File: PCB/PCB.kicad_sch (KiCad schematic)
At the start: 17 parts, among them SW1 SW_Push, SW2 SW_Push, SW3 SW_Push, SW4 SW_Push, SW5 SW_Push, SW6 SW_Push, U1 NodeMCU_1.0_(ESP-12E)

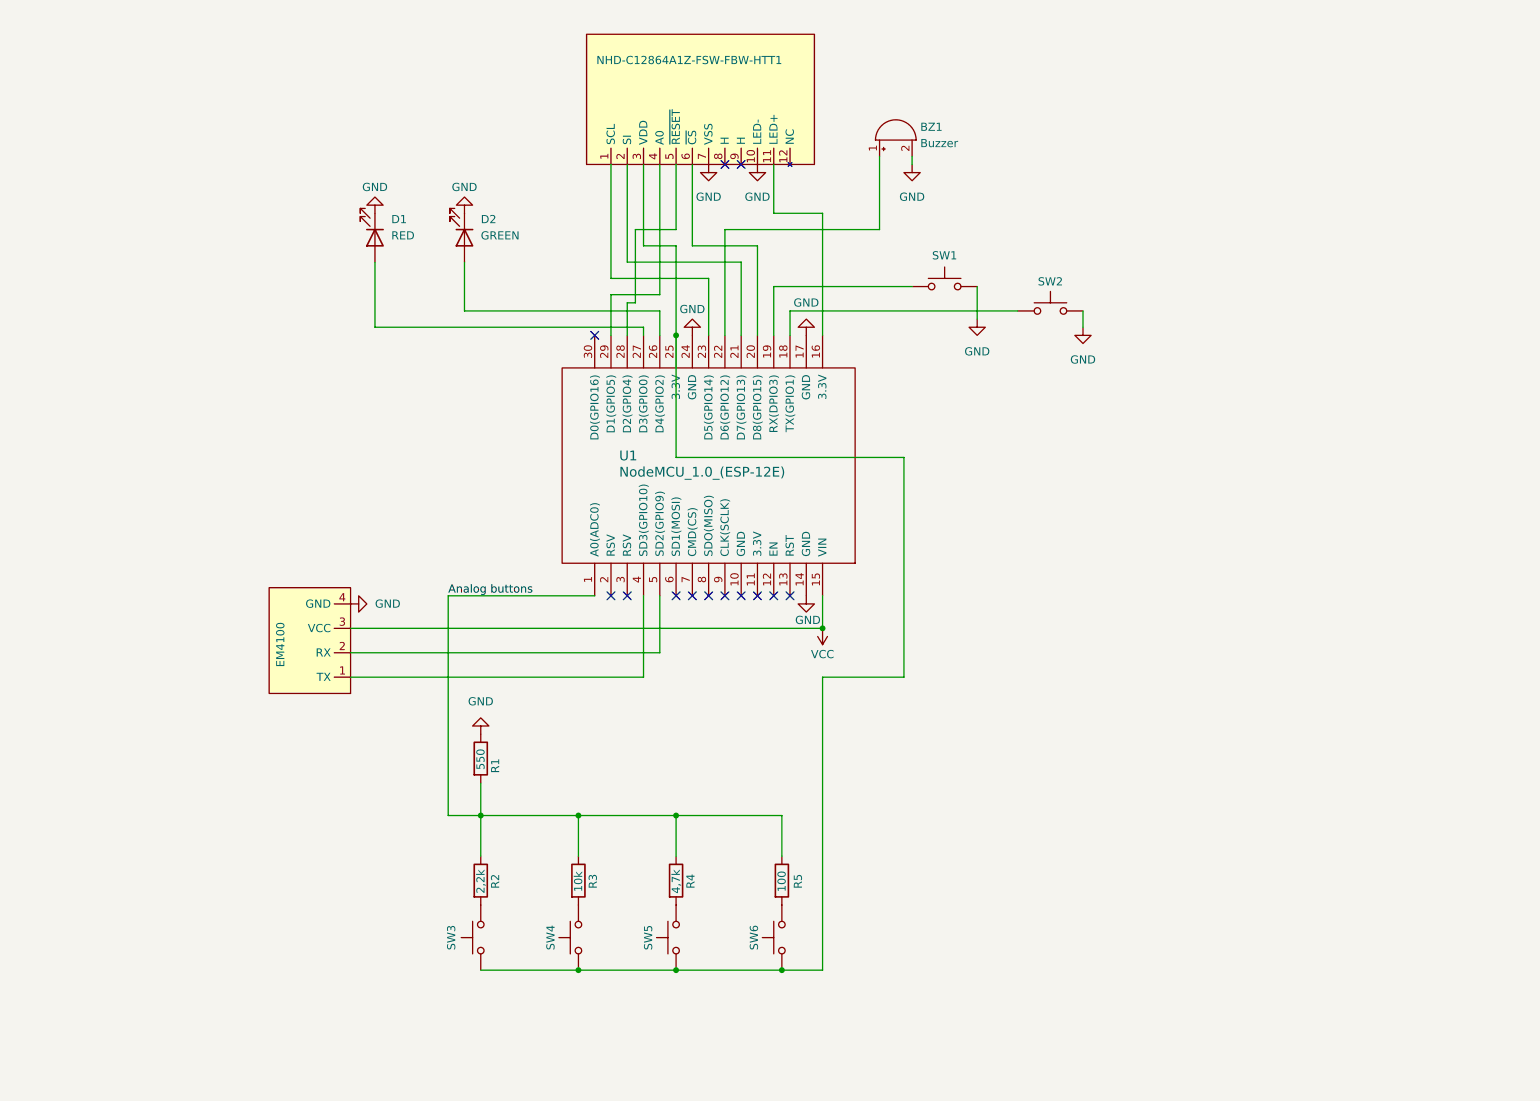
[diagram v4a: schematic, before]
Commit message: Updated schematic after CMZ feedback
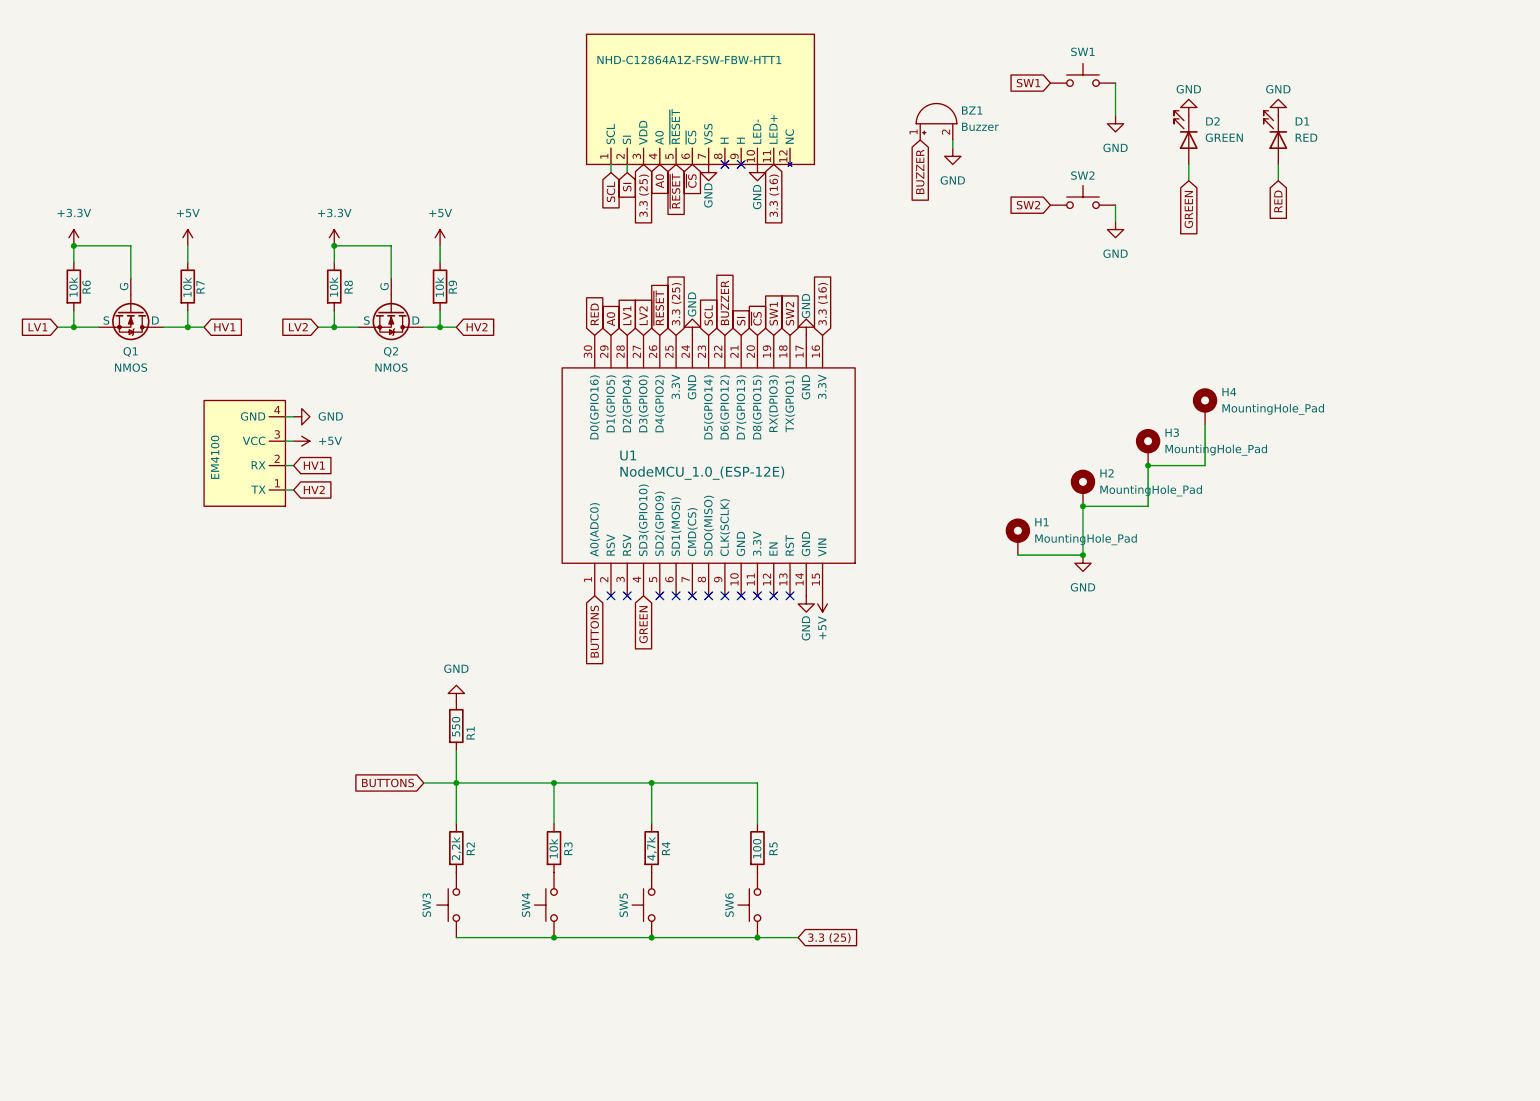
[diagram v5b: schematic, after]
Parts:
- added H1, H2, H3, H4: MountingHole_Pad, MountingHole:MountingHole_3.2mm_M3, symbol Mechanical:MountingHole_Pad
- added Q1, Q2: NMOS, symbol Simulation_SPICE:NMOS
- added R6, R7, R8, R9: 10k, symbol Device:R
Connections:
- net GND: now also H1.1, H2.1, H3.1, H4.1
- net LV2: now reaches U1.27 (D3(GPIO0))
- net LV2: now also Q2.3 (S), R8.2; no longer D1.2 (A)
- net SW1: now reaches SW1.1, U1.19 (RX(DPIO3))
- net SCL: now reaches NHD-C12864A1Z-FSW-FBW-HTT1.1 (SCL), U1.23 (D5(GPIO14))
- net 3.3 (16): now reaches NHD-C12864A1Z-FSW-FBW-HTT1.11 (LED+), U1.16 (3.3V)
- net SI: now reaches NHD-C12864A1Z-FSW-FBW-HTT1.2 (SI), U1.21 (D7(GPIO13))
- net 3.3 (25): now reaches NHD-C12864A1Z-FSW-FBW-HTT1.3 (VDD), SW3.1, SW4.1, SW5.1, SW6.1, U1.25 (3.3V)
- net A0: now reaches NHD-C12864A1Z-FSW-FBW-HTT1.4 (A0), U1.29 (D1(GPIO5))
- net LV1: now reaches U1.28 (D2(GPIO4))
- net LV1: now also Q1.3 (S), R6.2; no longer NHD-C12864A1Z-FSW-FBW-HTT1.5 (~{RESET})
- net ~{CS}: now reaches NHD-C12864A1Z-FSW-FBW-HTT1.6 (~{CS}), U1.20 (D8(GPIO15))
- net SW2: now reaches SW2.1, U1.18 (TX(GPIO1))
- net BUZZER: now reaches BZ1.1 (+), U1.22 (D6(GPIO12))
- net GREEN: now reaches U1.4 (SD3(GPIO10))
- net GREEN: now also D2.2 (A); no longer EM4100.1 (TX)
- net at U1.5 (SD2(GPIO9)): no longer EM4100.2 (RX)
- net ~{RESET}: now reaches U1.26 (D4(GPIO2))
- net ~{RESET}: now also NHD-C12864A1Z-FSW-FBW-HTT1.5 (~{RESET}); no longer D2.2 (A)
- net RED: now reaches U1.30 (D0(GPIO16))
- net RED: now also D1.2 (A)
- net Analog buttons renamed BUTTONS
- net VCC renamed +5V
- net +5V: now also R7.1, R9.1
- new net +3.3V: Q1.2 (G), Q2.2 (G), R6.1, R8.1
- new net HV1: EM4100.2 (RX), Q1.1 (D), R7.2
- new net HV2: EM4100.1 (TX), Q2.1 (D), R9.2
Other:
- moved on the sheet: BZ1, D1, D2, EM4100, R1, R2, R3, R4, R5, SW1, SW2, SW3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

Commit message: drawn new PCB based on feedback
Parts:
- Q1, Q2: footprint (none) -> Package_TO_SOT_THT:TO-92
- R1, R2, R3, R4, R5: footprint Resistor_SMD:R_1206_3216Metric_Pad1.30x1.75mm_HandSolder -> Resistor_THT:R_Axial_DIN0207_L6.3mm_D2.5mm_P7.62mm_Horizontal
- R6, R7, R8, R9: footprint (none) -> Resistor_THT:R_Axial_DIN0207_L6.3mm_D2.5mm_P7.62mm_Horizontal
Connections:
- net 3.3 (16) is gone; now on net +3.3V: NHD-C12864A1Z-FSW-FBW-HTT1.11 (LED+), U1.16 (3.3V)
- net 3.3 (25) is gone; now on net +3.3V: NHD-C12864A1Z-FSW-FBW-HTT1.3 (VDD), SW3.1, SW4.1, SW5.1, SW6.1, U1.25 (3.3V)
- net +3.3V: now also U1.11 (3.3V)
- net GND: now also U1.10 (GND)
- no-connect marks 13 -> 12
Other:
- moved on the sheet: H1, H2, H3, H4

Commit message: Fixed all errors and drawn tracks on 2nd layer
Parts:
- H1: footprint MountingHole:MountingHole_3.2mm_M3 -> MountingHole:MountingHole_3.2mm_M3_Pad
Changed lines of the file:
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@@
+	(wire
+		(pts
+			(xy 102.87 76.2) (xy 102.87 73.66)
+		)
+		(stroke
+			(width 0)
+			(type default)
+		)
+	)
+	(wire
+		(pts
+			(xy 95.25 63.5) (xy 86.36 63.5)
+		)
+		(stroke
+			(width 0)
+			(type default)
+		)
+	)
+	(wire
+		(pts
+			(xy 80.01 90.17) (xy 78.74 90.17)
+		)
+		(stroke
+			(width 0)
+			(type default)
+		)
+	)
+	(wire
+		(pts
+			(xy 246.38 100.33) (xy 224.79 100.33)
+		)
+		(stroke
+			(width 0)
+			(type default)
+		)
+	)
+	(wire
+		(pts
+			(xy 80.01 93.98) (xy 78.74 93.98)
+		)
+		(stroke
+			(width 0)
+			(type default)
+		)
+	)
 	(wire
 		(pts
 			(xy 78.74 97.79) (xy 80.01 97.79)
-		)
-		(stroke
-			(width 0)
-			(type default)
-		)
-	)
-	(wire
-		(pts
-			(xy 102.87 76.2) (xy 102.87 73.66)
-		)
-		(stroke
-			(width 0)
-			(type default)
-		)
-	)
-	(wire
-		(pts
-			(xy 95.25 63.5) (xy 86.36 63.5)
-		)
-		(stroke
-			(width 0)
-			(type default)
-		)
-	)
-	(wire
-		(pts
-			(xy 80.01 90.17) (xy 78.74 90.17)
-		)
-		(stroke
-			(width 0)
-			(type default)
-		)
-	)
-	(wire
-		(pts
-			(xy 246.38 100.33) (xy 224.79 100.33)
-		)
-		(stroke
-			(width 0)
-			(type default)
-		)
-	)
-	(wire
-		(pts
-			(xy 80.01 93.98) (xy 78.74 93.98)
 		)
 		(stroke
@@
 			)
 		)
-		(property "Footprint" "MountingHole:MountingHole_3.2mm_M3"
+		(property "Footprint" "MountingHole:MountingHole_3.2mm_M3_Pad"
 			(at 184.15 96.52 0)
 			(effects

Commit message: inital final
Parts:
- H2, H3, H4: footprint MountingHole:MountingHole_3.2mm_M3 -> MountingHole:MountingHole_3.2mm_M3_Pad
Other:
- moved on the sheet: H1
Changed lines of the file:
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@@
 	(title_block
 		(title "Meeting display")
-		(date "2024-04-24")
+		(date "2024-04-25")
 		(rev "0.3")
 		(company "KTH")
@@
 	)
 	(junction
-		(at 86.36 63.5)
+		(at 160.02 63.5)
 		(diameter 0)
 		(color 0 0 0 0)
 	)
 	(junction
-		(at 152.4 171.45)
+		(at 86.36 63.5)
 		(diameter 0)
 		(color 0 0 0 0)
 	)
 	(junction
-		(at 45.72 76.2)
+		(at 152.4 171.45)
 		(diameter 0)
 		(color 0 0 0 0)
 	)
 	(junction
-		(at 165.1 66.04)
+		(at 45.72 76.2)
 		(diameter 0)
 		(color 0 0 0 0)
@@
 	(wire
 		(pts
-			(xy 184.15 100.33) (xy 204.47 100.33)
-		)
-		(stroke
-			(width 0)
-			(type default)
-		)
-	)
-	(wire
-		(pts
-			(xy 165.1 67.31) (xy 165.1 66.04)
+			(xy 182.88 100.33) (xy 204.47 100.33)
 		)
 		(stroke
@@
 	(wire
 		(pts
-			(xy 165.1 66.04) (xy 160.02 66.04)
-		)
-		(stroke
-			(width 0)
-			(type default)
-		)
-	)
-	(wire
-		(pts
 			(xy 83.82 76.2) (xy 86.36 76.2)
 		)
@@
 	(wire
 		(pts
-			(xy 184.15 99.06) (xy 184.15 100.33)
+			(xy 182.88 99.06) (xy 182.88 100.33)
 		)
 		(stroke
@@
 	(wire
 		(pts
-			(xy 160.02 66.04) (xy 160.02 77.47)
+			(xy 160.02 63.5) (xy 160.02 77.47)
 		)
 		(stroke
@@
 	(wire
 		(pts
+			(xy 162.56 73.66) (xy 162.56 77.47)
+		)
+		(stroke
+			(width 0)
+			(type default)
+		)
+	)
+	(wire
+		(pts
 			(xy 120.65 147.32) (xy 120.65 153.67)
 		)
@@
 	)
 	(symbol
-		(lib_id "power:PWR_FLAG")
-		(at 165.1 67.31 180)
-		(unit 1)
-		(exclude_from_sim no)
-		(in_bom yes)
-		(on_board yes)
-		(dnp no)
-		(property "Reference" "#FLG02"
-			(at 165.1 69.215 0)
-			(effects
-				(font
-					(size 1.27 1.27)
-				)
-				(hide yes)
-			)
-		)
-		(property "Value" "PWR_FLAG"
-			(at 168.656 71.628 0)
-			(effects
-				(font
-					(size 1.27 1.27)
-				)
-			)
-		)
-		(property "Footprint" ""
-			(at 165.1 67.31 0)
-			(effects
-				(font
-					(size 1.27 1.27)
-				)
-				(hide yes)
-			)
-		)
-		(property "Datasheet" "~"
-			(at 165.1 67.31 0)
-			(effects
-				(font
-					(size 1.27 1.27)
-				)
-				(hide yes)
-			)
-		)
-		(property "Description" "Special symbol for telling ERC where power comes from"
-			(at 165.1 67.31 0)
-			(effects
-				(font
-					(size 1.27 1.27)
-				)
-				(hide yes)
-			)
-		)
-		(pin "1"
-		)
-		(instances
-			(project "PCB"
-				(path "/95b5e99e-302e-4222-afa1-0faa09b15eb9"
-					(reference "#FLG02")
-					(unit 1)
-				)
-			)
-		)
-	)
-	(symbol
 		(lib_id "power:+5V")
 		(at 63.5 63.5 0)
@@
 	(symbol
 		(lib_id "power:+3.3V")
-		(at 162.56 77.47 0)
+		(at 162.56 73.66 0)
 		(unit 1)
 		(exclude_from_sim no)
@@
 		(dnp no)
 		(property "Reference" "#PWR018"
-			(at 162.56 81.28 0)
+			(at 162.56 77.47 0)
 			(effects
 				(font
@@
 		)
 		(property "Value" "+3.3V"
-			(at 162.56 71.882 90)
+			(at 162.56 68.072 90)
 			(effects
 				(font
@@
 		)
 		(property "Footprint" ""
-			(at 162.56 77.47 0)
+			(at 162.56 73.66 0)
 			(effects
 				(font
@@
 		)
 		(property "Datasheet" ""
-			(at 162.56 77.47 0)
+			(at 162.56 73.66 0)
 			(effects
 				(font
@@
 		)
 		(property "Description" "Power symbol creates a global label with name \"+3.3V\""
-			(at 162.56 77.47 0)
+			(at 162.56 73.66 0)
 			(effects
 				(font
@@
 	(symbol
 		(lib_id "Mechanical:MountingHole_Pad")
-		(at 184.15 96.52 0)
+		(at 182.88 96.52 0)
 		(unit 1)
 		(exclude_from_sim yes)
@@
 		(dnp no)
 		(property "Reference" "H1"
-			(at 186.69 93.9799 0)
+			(at 185.42 93.9799 0)
 			(effects
 				(font
@@
 		)
 		(property "Value" "MountingHole_Pad"
-			(at 186.69 96.5199 0)
+			(at 185.42 96.5199 0)
 			(effects
 				(font
@@
 		)
 		(property "Footprint" "MountingHole:MountingHole_3.2mm_M3_Pad"
-			(at 184.15 96.52 0)
+			(at 182.88 96.52 0)
 			(effects
 				(font
@@
 		)
 		(property "Datasheet" "~"
-			(at 184.15 96.52 0)
+			(at 182.88 96.52 0)
 			(effects
 				(font
@@
 		)
 		(property "Description" "Mounting Hole with connection"
-			(at 184.15 96.52 0)
+			(at 182.88 96.52 0)
 			(effects
 				(font
@@
 			)
 		)
-		(property "Footprint" "MountingHole:MountingHole_3.2mm_M3"
+		(property "Footprint" "MountingHole:MountingHole_3.2mm_M3_Pad"
 			(at 246.38 82.55 0)
 			(effects
@@
 			)
 		)
-		(property "Footprint" "MountingHole:MountingHole_3.2mm_M3"
+		(property "Footprint" "MountingHole:MountingHole_3.2mm_M3_Pad"
 			(at 224.79 85.09 0)
 			(effects
@@
 	)
 	(symbol
+		(lib_id "power:PWR_FLAG")
+		(at 160.02 63.5 0)
+		(unit 1)
+		(exclude_from_sim no)
+		(in_bom yes)
+		(on_board yes)
+		(dnp no)
+		(property "Reference" "#FLG02"
+			(at 160.02 61.595 0)
+			(effects
+				(font
+					(size 1.27 1.27)
+				)
+				(hide yes)
+			)
+		)
+		(property "Value" "PWR_FLAG"
+			(at 163.83 59.182 0)
+			(effects
+				(font
+					(size 1.27 1.27)
+				)
+			)
+		)
+		(property "Footprint" ""
+			(at 160.02 63.5 0)
+			(effects
+				(font
+					(size 1.27 1.27)
+				)
+				(hide yes)
+			)
+		)
+		(property "Datasheet" "~"
+			(at 160.02 63.5 0)
+			(effects
+				(font
+					(size 1.27 1.27)
+				)
+				(hide yes)
+			)
+		)
+		(property "Description" "Special symbol for telling ERC where power comes from"
+			(at 160.02 63.5 0)
+			(effects
+				(font
+					(size 1.27 1.27)
+				)
+				(hide yes)
+			)
+		)
+		(pin "1"
+		)
+		(instances
+			(project "PCB"
+				(path "/95b5e99e-302e-4222-afa1-0faa09b15eb9"
+					(reference "#FLG02")
+					(unit 1)
+				)
+			)
+		)
+	)
+	(symbol
 		(lib_id "power:GND")
-		(at 165.1 66.04 90)
+		(at 160.02 63.5 90)
 		(unit 1)
 		(exclude_from_sim no)
@@
 		(dnp no)
 		(property "Reference" "#PWR02"
-			(at 171.45 66.04 0)
+			(at 166.37 63.5 0)
 			(effects
 				(font
@@
 		)
 		(property "Value" "GND"
-			(at 170.18 66.04 90)
+			(at 165.1 63.5 90)
 			(effects
 				(font
@@
 		)
 		(property "Footprint" ""
-			(at 165.1 66.04 0)
+			(at 160.02 63.5 0)
 			(effects
 				(font
@@
 		)
 		(property "Datasheet" ""
-			(at 165.1 66.04 0)
+			(at 160.02 63.5 0)
 			(effects
 				(font
@@
 		)
 		(property "Description" "Power symbol creates a global label with name \"GND\" , ground"
-			(at 165.1 66.04 0)
+			(at 160.02 63.5 0)
 			(effects
 				(font
@@
 			)
 		)
-		(property "Footprint" "MountingHole:MountingHole_3.2mm_M3"
+		(property "Footprint" "MountingHole:MountingHole_3.2mm_M3_Pad"
 			(at 204.47 90.17 0)
 			(effects
